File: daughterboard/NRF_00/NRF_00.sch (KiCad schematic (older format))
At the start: 2 parts, among them J1 m2_keyA_67pin_daughterboard

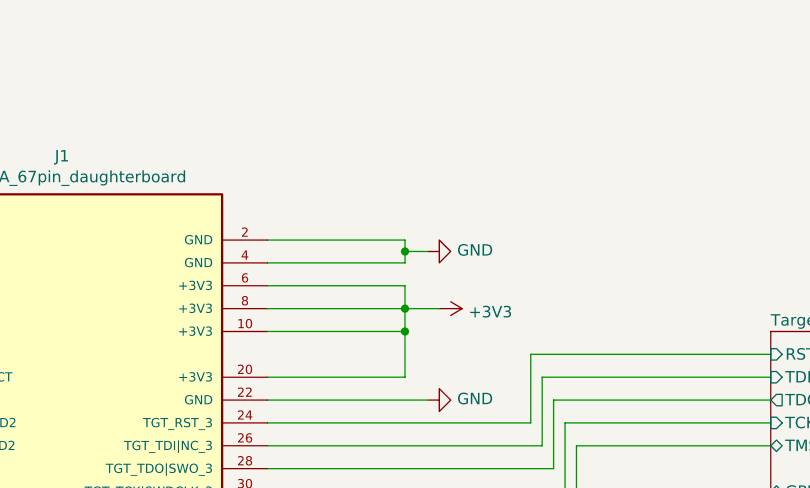
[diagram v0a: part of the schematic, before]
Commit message: finished NRF daughterboard schematics
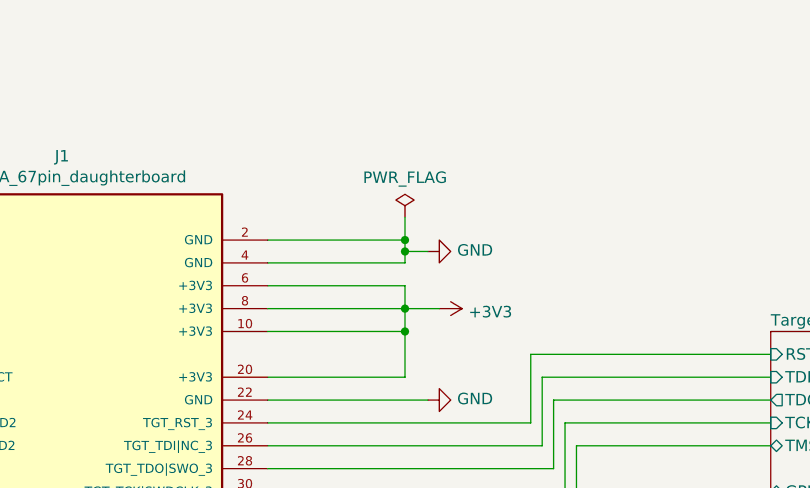
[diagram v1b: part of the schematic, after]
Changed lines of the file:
@@
 	0    -1   -1   0
 $EndComp
+$Comp
+L power:PWR_FLAG #FLG0101
+U 1 1 619EA201
+P 7500 1500
+F 0 "#FLG0101" H 7500 1575 50  0001 C CNN
+F 1 "PWR_FLAG" H 7500 1673 50  0000 C CNN
+F 2 "" H 7500 1500 50  0001 C CNN
+F 3 "~" H 7500 1500 50  0001 C CNN
+	1    7500 1500
+	1    0    0    -1
+$EndComp
+Wire Wire Line
+	7500 1600 7500 1500
+Connection ~ 7500 1600
 $EndSCHEMATC
